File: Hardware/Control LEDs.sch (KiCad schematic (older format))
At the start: 8 parts

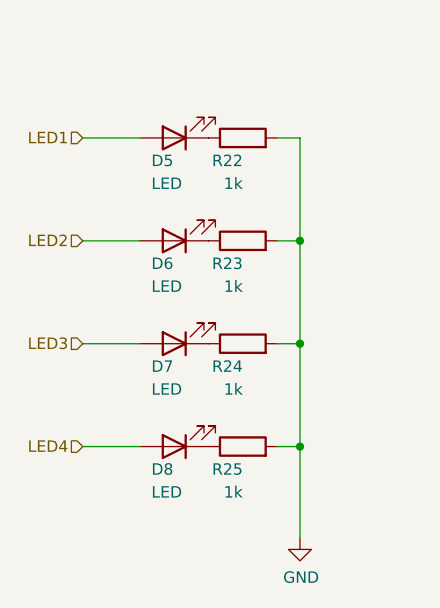
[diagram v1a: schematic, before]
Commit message: controll leds are now groundend on uC, some changes of the pcb layout
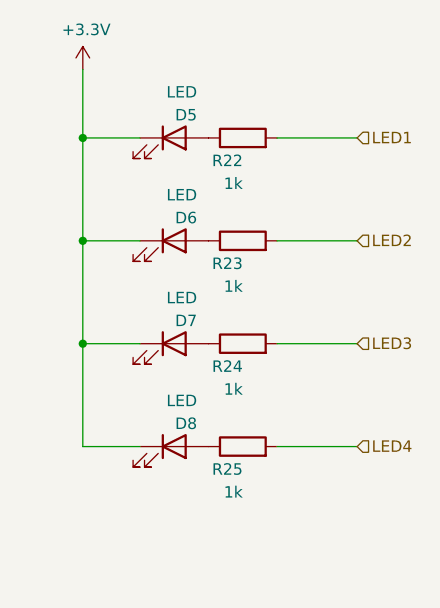
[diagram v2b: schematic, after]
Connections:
- net LED1: now also R22.2; no longer D5.2 (A)
- net LED2: now also R23.2; no longer D6.2 (A)
- net LED3: now also R24.2; no longer D7.2 (A)
- net LED4: now also R25.2; no longer D8.2 (A)
- net at R25.1: now also D8.2 (A); no longer D8.1 (K)
- net at R24.1: now also D7.2 (A); no longer D7.1 (K)
- net at R23.1: now also D6.2 (A); no longer D6.1 (K)
- net at R22.1: now also D5.2 (A); no longer D5.1 (K)
- removed net GND: R22.2, R23.2, R24.2, R25.2
- new net +3V3: D5.1 (K), D6.1 (K), D7.1 (K), D8.1 (K)
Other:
- moved on the sheet: D5, D6, D7, D8
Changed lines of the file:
@@
 F 3 "~" H 4700 4250 50  0001 C CNN
 	1    4700 4250
-	-1   0    0    1
+	1    0    0    -1
 $EndComp
 $Comp
@@
 $EndComp
 $Comp
-L power:GND #PWR?
-U 1 1 61CB95DC
-P 5250 4650
-AR Path="/61A6380E/61CB95DC" Ref="#PWR?"  Part="1"
-AR Path="/61C66CAF/61CB95DC" Ref="#PWR06"  Part="1"
-F 0 "#PWR06" H 5250 4400 50  0001 C CNN
-F 1 "GND" H 5255 4477 50  0000 C CNN
-F 2 "" H 5250 4650 50  0001 C CNN
-F 3 "" H 5250 4650 50  0001 C CNN
-	1    5250 4650
-	1    0    0    -1
-$EndComp
-$Comp
 L Device:LED D?
 U 1 1 61CBC6B8
@@
 F 3 "~" H 4700 3800 50  0001 C CNN
 	1    4700 3800
-	-1   0    0    1
+	1    0    0    -1
 $EndComp
 $Comp
@@
 F 3 "~" H 4700 3350 50  0001 C CNN
 	1    4700 3350
-	-1   0    0    1
+	1    0    0    -1
 $EndComp
 $Comp
@@
 F 3 "~" H 4700 2900 50  0001 C CNN
 	1    4700 2900
-	-1   0    0    1
+	1    0    0    -1
 $EndComp
 $Comp
@@
 	0    -1   -1   0
 $EndComp
+Text HLabel 5500 2900 2    50   Input ~ 0
+LED1
+Text HLabel 5500 3350 2    50   Input ~ 0
+LED2
+Text HLabel 5500 3800 2    50   Input ~ 0
+LED3
+Text HLabel 5500 4250 2    50   Input ~ 0
+LED4
 Wire Wire Line
-	5250 4250 5250 4650
+	5150 2900 5500 2900
 Wire Wire Line
-	5250 4250 5150 4250
+	5150 3800 5500 3800
 Wire Wire Line
-	5150 3800 5250 3800
-Connection ~ 5250 3800
+	5150 4250 5500 4250
 Wire Wire Line
-	5250 3800 5250 4250
+	5150 3350 5500 3350
+$Comp
+L power:+3.3V #PWR?
+U 1 1 61C9EAAD
+P 4300 2600
+F 0 "#PWR?" H 4300 2450 50  0001 C CNN
+F 1 "+3.3V" H 4315 2773 50  0000 C CNN
+F 2 "" H 4300 2600 50  0001 C CNN
+F 3 "" H 4300 2600 50  0001 C CNN
+	1    4300 2600
+	1    0    0    -1
+$EndComp
 Wire Wire Line
-	5150 3350 5250 3350
-Connection ~ 5250 3350
+	4300 2600 4300 2900
 Wire Wire Line
-	5250 3350 5250 3800
+	4550 2900 4300 2900
+Connection ~ 4300 2900
 Wire Wire Line
-	5150 2900 5250 2900
+	4300 2900 4300 3350
 Wire Wire Line
-	5250 2900 5250 3350
-Connection ~ 5250 4250
+	4550 3350 4300 3350
+Connection ~ 4300 3350
 Wire Wire Line
-	4300 2900 4550 2900
+	4300 3350 4300 3800
 Wire Wire Line
-	4300 3350 4550 3350
+	4550 3800 4300 3800
+Connection ~ 4300 3800
 Wire Wire Line
-	4300 3800 4550 3800
+	4550 4250 4300 4250
 Wire Wire Line
-	4300 4250 4550 4250
-Text HLabel 4300 2900 0    50   Input ~ 0
-LED1
-Text HLabel 4300 3350 0    50   Input ~ 0
-LED2
-Text HLabel 4300 3800 0    50   Input ~ 0
-LED3
-Text HLabel 4300 4250 0    50   Input ~ 0
-LED4
+	4300 3800 4300 4250
 $EndSCHEMATC
